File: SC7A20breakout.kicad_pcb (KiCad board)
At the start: 2 copper layers, 25.4 x 25.4 mm, 36 parts, among them J1 Qwiic_I2C_connector, J2 Qwiic_I2C_connector, J3 Conn_01x04, J4 Conn_01x04, U1 SC7A20

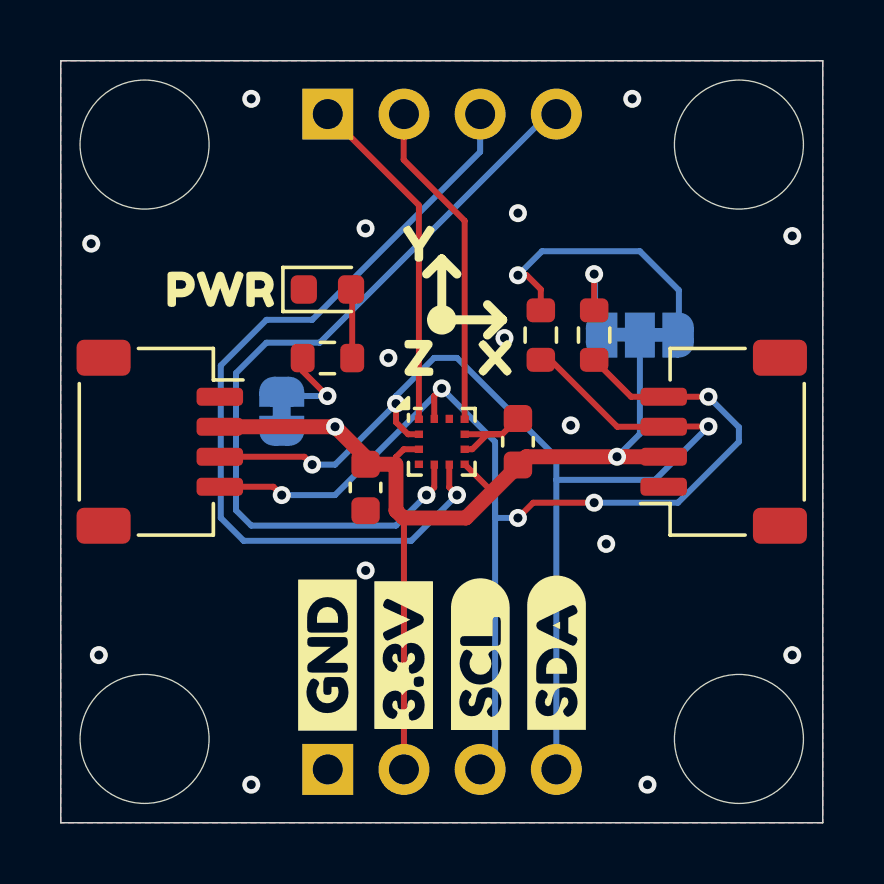
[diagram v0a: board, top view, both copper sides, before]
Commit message: Correct hole spacing and labeling
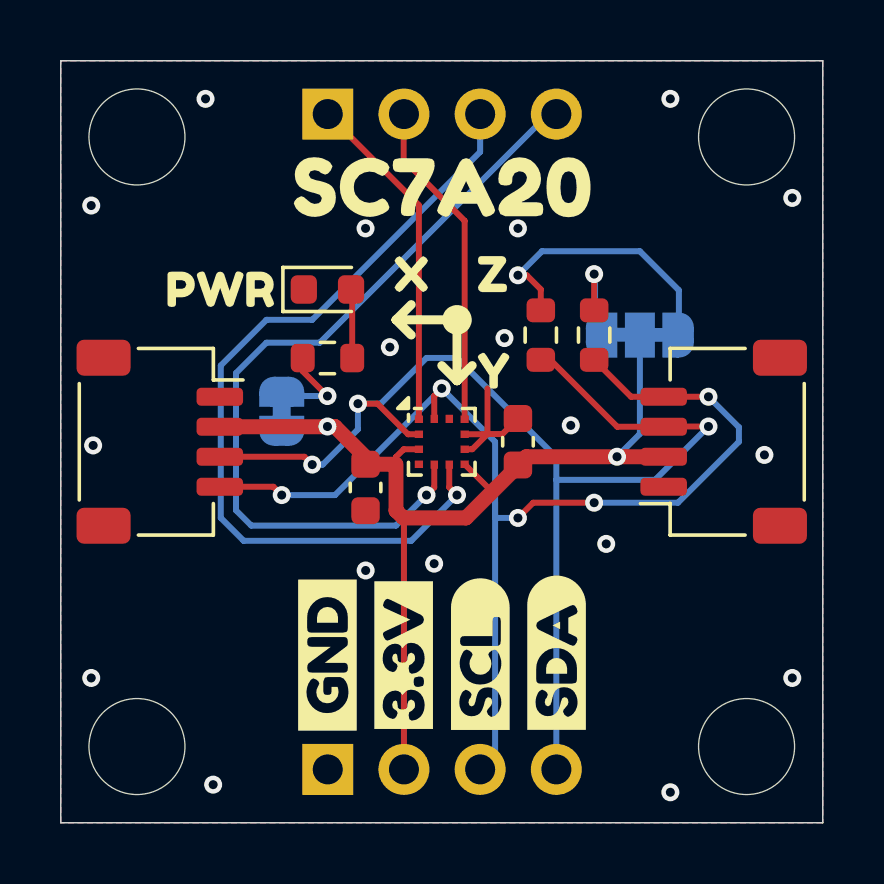
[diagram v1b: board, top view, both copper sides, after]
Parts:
- removed kibuzzard-667CFF16: G***, kibuzzard-667CFF16
- removed kibuzzard-667D0235: G***, kibuzzard-667D0235
- added kibuzzard-667DD6C5: G***, kibuzzard-667DD6C5, F.Cu at (111.8, 68.2)
- added kibuzzard-667DDCB5: G***, kibuzzard-667DDCB5, B.Cu at (103.4, 82.3)
- added kibuzzard-667DE64B: G***, kibuzzard-667DE64B, B.Cu at (103.9, 69.8)
- added kibuzzard-667DE68B: G***, kibuzzard-667DE68B, B.Cu at (123.4, 77.0)
- added kibuzzard-667DFE26: G***, kibuzzard-667DFE26, B.Cu at (118.4, 70.1)
- added kibuzzard-667DFE33: G***, kibuzzard-667DFE33, B.Cu at (120.6, 77.4)
- H1, H2, H3, H4: footprint MountingHole:MountingHole_4.3mm_M4 -> MountingHole:MountingHole_3.2mm_M3
- R1: value R_US -> 1k
- moved kibuzzard-667D053C 4.91 mm to (113.5, 74.3)
- moved kibuzzard-667D0544 3.95 mm to (110.7, 71.1)
- moved kibuzzard-667D0532 3.72 mm to (113.5, 71.1)
- moved H4 0.36 mm to (121.9, 66.5)
- moved H3 0.36 mm to (121.9, 86.9)
- moved H1 0.36 mm to (101.6, 66.5)
- moved H2 0.36 mm to (101.6, 86.9)
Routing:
- net /SDA/MOSI: track 38.8 -> 40.1 mm
- net GND: track 3.45 -> 4.48 mm, vias 15 -> 18
